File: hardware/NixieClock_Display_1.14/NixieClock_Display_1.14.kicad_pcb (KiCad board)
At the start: 2 copper layers, 17.5 x 41.9 mm, 2 parts, among them J1 Conn_01x08, J2 Conn_01x08

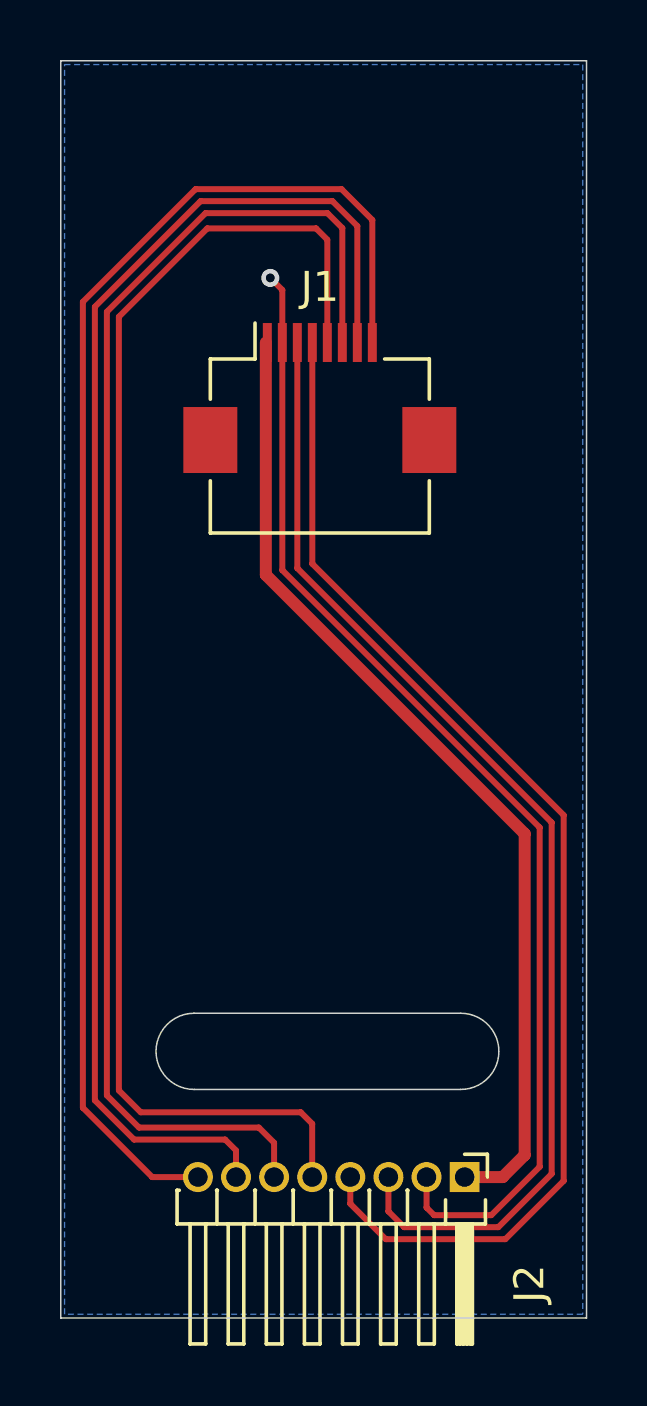
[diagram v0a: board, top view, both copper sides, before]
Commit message: display 1.14 anpassungen. Stecker war verpolt
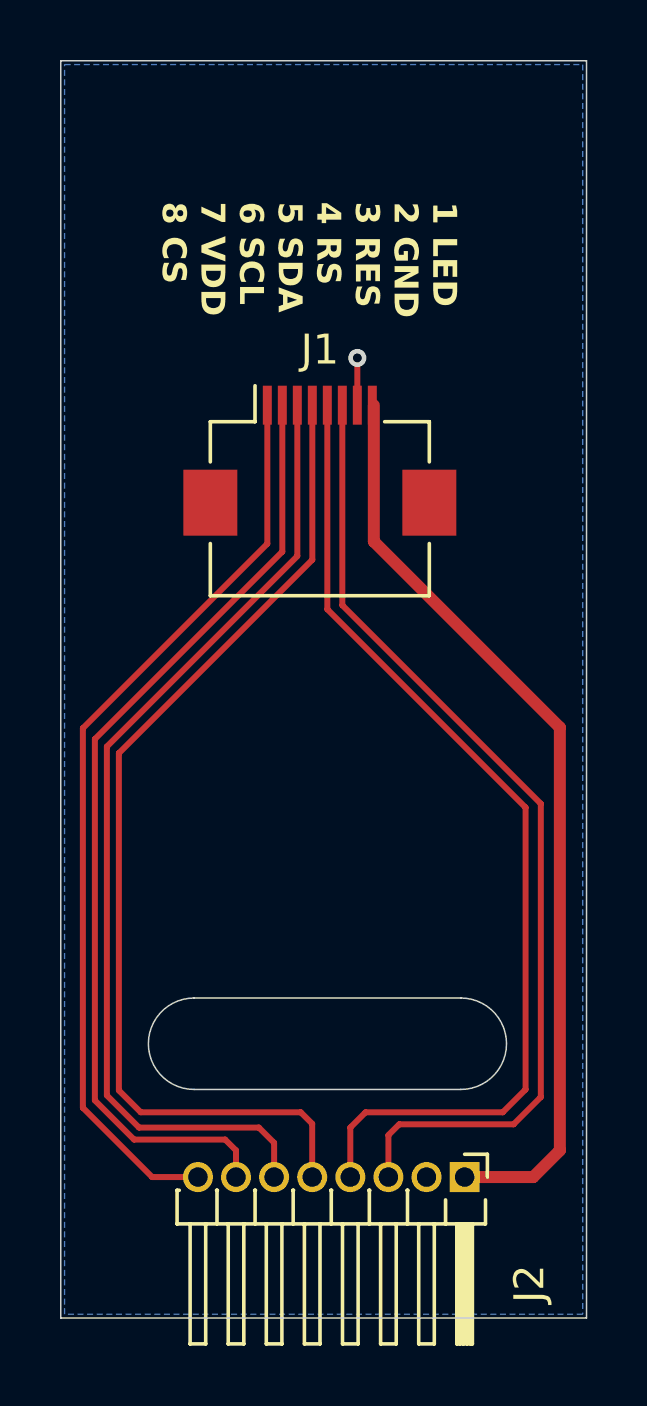
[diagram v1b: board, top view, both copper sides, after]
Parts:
- moved J1 2.09 mm to (135.6, 74.3)
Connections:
- J1 pad 1: /LEDA -> /CS
- J1 pad 2: /GND -> /VDD
- J1 pad 3: /RESET -> /SCL
- J1 pad 4: /RS -> /SDA
- J1 pad 5: /SDA -> /RS
- J1 pad 6: /SCL -> /RESET
- J1 pad 7: /VDD -> /GND
- J1 pad 8: /CS -> /LEDA
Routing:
- net /GND: track 38.9 -> 1.58 mm
- net /CS: track 46.9 -> 30.8 mm
- net /VDD: track 46.7 -> 32.0 mm
- net /SCL: track 46.2 -> 33.0 mm
- net /SDA: track 45.7 -> 34.2 mm
- net /RS: track 41.2 -> 33.6 mm
- net /RESET: track 39.3 -> 32.8 mm
- net /LEDA: track 33.0 -> 31.0 mm
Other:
- outline, holes or cut-outs redrawn
